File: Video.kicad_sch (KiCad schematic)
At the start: 53 parts, among them Q10 2N3904, Q6 2N3904, Q7 2N3904, Q8 2N3904, Q9 2N3904, U13 74LS04, U15 74LS86, U40 GST_SHIFTER, U41 74LS257, U42 GST_MCU, U44 74LS86, U45 74LS04

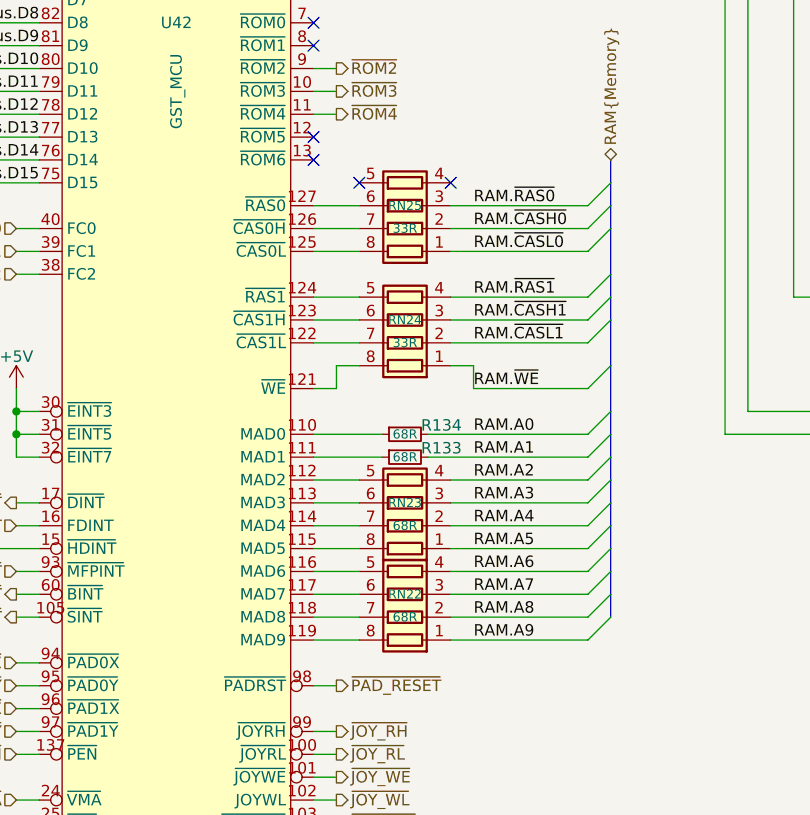
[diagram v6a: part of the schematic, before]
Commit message: motherboard: Fixed a pile of resistor network issues, and concluded initial routing of the CPU and audio amp passives
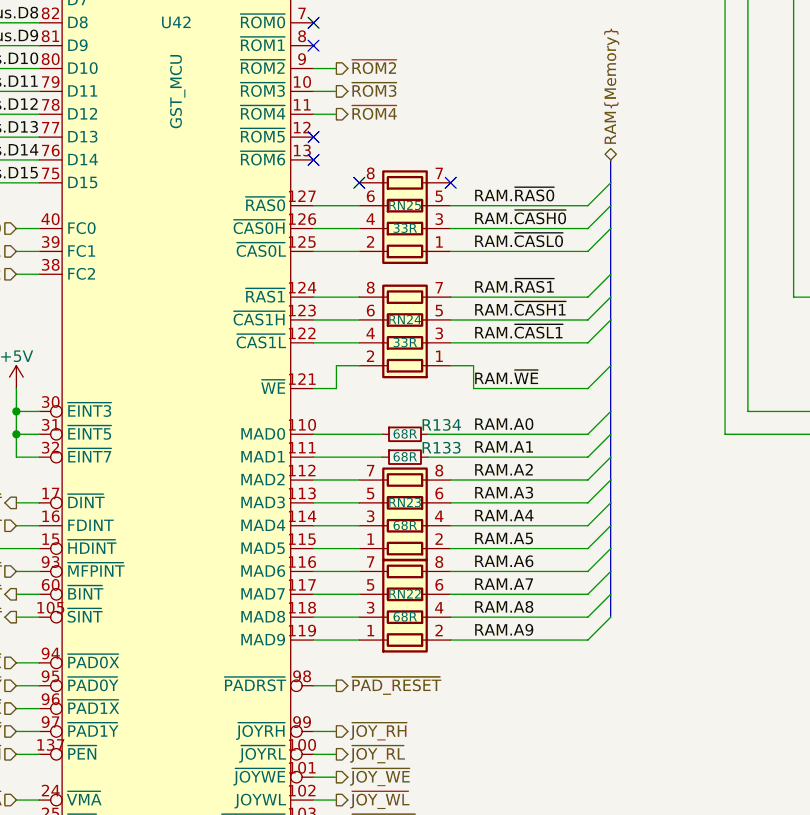
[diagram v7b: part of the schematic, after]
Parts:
- R133, R134: footprint rhais_rcl:R0603 -> rhais_rcl:R0402
- RN22, RN23, RN24, RN25: footprint rhais_rcl:R0603_Array_Concave_4 -> rhais_rcl:R0402_Array_Convex_4; symbol Device:R_Pack04 -> dragonmux:R_Pack04_OddEven
- U40: footprint Package_LCC:PLCC-84_SMD-Socket -> rhais_package-plcc:PLCC-84_SMD-Socket
- U42: footprint Package_QFP:LQFP-144_20x20mm_P0.5mm -> rhais_package-qfp:LQFP-144_20x20mm_P0.5mm
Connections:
- net RAM.A2: now also RN23.8 (R1.2); no longer RN23.4 (R4.1)
- net RAM.A3: now also RN23.6 (R3.2); no longer RN23.3 (R3.1)
- net RAM.A4: now also RN23.4 (R4.1); no longer RN23.2 (R2.1)
- net RAM.A5: now also RN23.2 (R2.1); no longer RN23.1 (R1.1)
- net RAM.A6: now also RN22.8 (R1.2); no longer RN22.4 (R4.1)
- net RAM.A7: now also RN22.6 (R3.2); no longer RN22.3 (R3.1)
- net RAM.A8: now also RN22.4 (R4.1); no longer RN22.2 (R2.1)
- net RAM.A9: now also RN22.2 (R2.1); no longer RN22.1 (R1.1)
- net RAM.~{CASH0}: now also RN25.3 (R3.1); no longer RN25.2 (R2.1)
- net RAM.~{CASH1}: now also RN24.5 (R4.2); no longer RN24.3 (R3.1)
- net RAM.~{CASL1}: now also RN24.3 (R3.1); no longer RN24.2 (R2.1)
- net RAM.~{RAS0}: now also RN25.5 (R4.2); no longer RN25.3 (R3.1)
- net RAM.~{RAS1}: now also RN24.7 (R2.2); no longer RN24.4 (R4.1)
- net at RN25.4 (R4.1): now also U42.126 (~{CAS0H})
- net at RN25.7 (R2.2): no longer U42.126 (~{CAS0H})
- net at U42.125 (~{CAS0L}): now also RN25.2 (R2.1); no longer RN25.8 (R1.2)
- net at U42.112 (MAD2): now also RN23.7 (R2.2); no longer RN23.5 (R4.2)
- net at U42.113 (MAD3): now also RN23.5 (R4.2); no longer RN23.6 (R3.2)
- net at U42.114 (MAD4): now also RN23.3 (R3.1); no longer RN23.7 (R2.2)
- net at U42.115 (MAD5): now also RN23.1 (R1.1); no longer RN23.8 (R1.2)
- net at U42.116 (MAD6): now also RN22.7 (R2.2); no longer RN22.5 (R4.2)
- net at U42.117 (MAD7): now also RN22.5 (R4.2); no longer RN22.6 (R3.2)
- net at U42.118 (MAD8): now also RN22.3 (R3.1); no longer RN22.7 (R2.2)
- net at U42.119 (MAD9): now also RN22.1 (R1.1); no longer RN22.8 (R1.2)
- net at U42.121 (~{WE}): now also RN24.2 (R2.1); no longer RN24.8 (R1.2)
- net at U42.122 (~{CAS1L}): now also RN24.4 (R4.1); no longer RN24.7 (R2.2)
- net at U42.124 (~{RAS1}): now also RN24.8 (R1.2); no longer RN24.5 (R4.2)
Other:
- moved on the sheet: RN22, RN23
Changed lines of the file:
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@@
 			)
 		)
-		(property "Footprint" "Package_LCC:PLCC-84_SMD-Socket"
+		(property "Footprint" "rhais_package-plcc:PLCC-84_SMD-Socket"
 			(at 218.44 127 90)
 			(effects
@@
 			)
 		)
+		(property "MFR" ""
+			(at 215.9 127 0)
+			(effects
+				(font
+					(size 1.27 1.27)
+				)
+				(hide yes)
+			)
+		)
+		(property "MPN" ""
+			(at 215.9 127 0)
+			(effects
+				(font
+					(size 1.27 1.27)
+				)
+				(hide yes)
+			)
+		)
+		(property "OC_FARNELL" ""
+			(at 215.9 127 0)
+			(effects
+				(font
+					(size 1.27 1.27)
+				)
+				(hide yes)
+			)
+		)
 		(pin "61"
 		)
@@
 			)
 		)
-		(property "Footprint" "rhais_rcl:R0603"
+		(property "Footprint" "rhais_rcl:R0402"
 			(at 114.3 193.04 0)
 			(effects
@@
 	)
 	(symbol
-		(lib_id "Device:R_Pack04")
+		(lib_id "dragonmux:R_Pack04_OddEven")
 		(at 114.3 165.1 90)
 		(unit 1)
@@
 			)
 		)
-		(property "Footprint" "rhais_rcl:R0603_Array_Concave_4"
+		(property "Footprint" "rhais_rcl:R0402_Array_Convex_4"
 			(at 114.3 158.115 90)
 			(effects
@@
 		)
 		(property "Description" "4 resistor network, parallel topology"
-			(at 114.3 165.1 0)
+			(at 127 166.37 0)
 			(effects
 				(font
@@
 			)
 		)
-		(property "Footprint" "Package_QFP:LQFP-144_20x20mm_P0.5mm"
+		(property "Footprint" "rhais_package-qfp:LQFP-144_20x20mm_P0.5mm"
 			(at 91.694 152.4 90)
 			(effects
@@
 			)
 		)
+		(property "MFR" ""
+			(at 88.9 152.4 0)
+			(effects
+				(font
+					(size 1.27 1.27)
+				)
+				(hide yes)
+			)
+		)
+		(property "MPN" ""
+			(at 88.9 152.4 0)
+			(effects
+				(font
+					(size 1.27 1.27)
+				)
+				(hide yes)
+			)
+		)
+		(property "OC_FARNELL" ""
+			(at 88.9 152.4 0)
+			(effects
+				(font
+					(size 1.27 1.27)
+				)
+				(hide yes)
+			)
+		)
 		(pin "55"
 		)
@@
 	)
 	(symbol
-		(lib_id "Device:R_Pack04")
+		(lib_id "dragonmux:R_Pack04_OddEven")
 		(at 114.3 177.8 90)
 		(unit 1)
@@
 			)
 		)
-		(property "Footprint" "rhais_rcl:R0603_Array_Concave_4"
+		(property "Footprint" "rhais_rcl:R0402_Array_Convex_4"
 			(at 114.3 170.815 90)
 			(effects
@@
 		)
 		(property "Description" "4 resistor network, parallel topology"
-			(at 114.3 177.8 0)
+			(at 127 179.07 0)
 			(effects
 				(font
@@
 	)
 	(symbol
-		(lib_id "Device:R_Pack04")
-		(at 114.3 198.12 90)
+		(lib_id "dragonmux:R_Pack04_OddEven")
+		(at 114.3 198.12 270)
+		(mirror x)
 		(unit 1)
 		(exclude_from_sim no)
@@
 			)
 		)
-		(property "Footprint" "rhais_rcl:R0603_Array_Concave_4"
+		(property "Footprint" "rhais_rcl:R0402_Array_Convex_4"
 			(at 114.3 191.135 90)
 			(effects
@@
 		)
 		(property "Description" "4 resistor network, parallel topology"
-			(at 114.3 198.12 0)
+			(at 101.6 199.39 0)
 			(effects
 				(font
@@
 			)
 		)
-		(property "Footprint" "rhais_rcl:R0603"
+		(property "Footprint" "rhais_rcl:R0402"
 			(at 114.3 190.5 0)
 			(effects
@@
 	)
 	(symbol
-		(lib_id "Device:R_Pack04")
-		(at 114.3 208.28 90)
+		(lib_id "dragonmux:R_Pack04_OddEven")
+		(at 114.3 208.28 270)
+		(mirror x)
 		(unit 1)
 		(exclude_from_sim no)
@@
 			)
 		)
-		(property "Footprint" "rhais_rcl:R0603_Array_Concave_4"
+		(property "Footprint" "rhais_rcl:R0402_Array_Convex_4"
 			(at 114.3 201.295 90)
 			(effects
@@
 		)
 		(property "Description" "4 resistor network, parallel topology"
-			(at 114.3 208.28 0)
+			(at 101.6 209.55 0)
 			(effects
 				(font

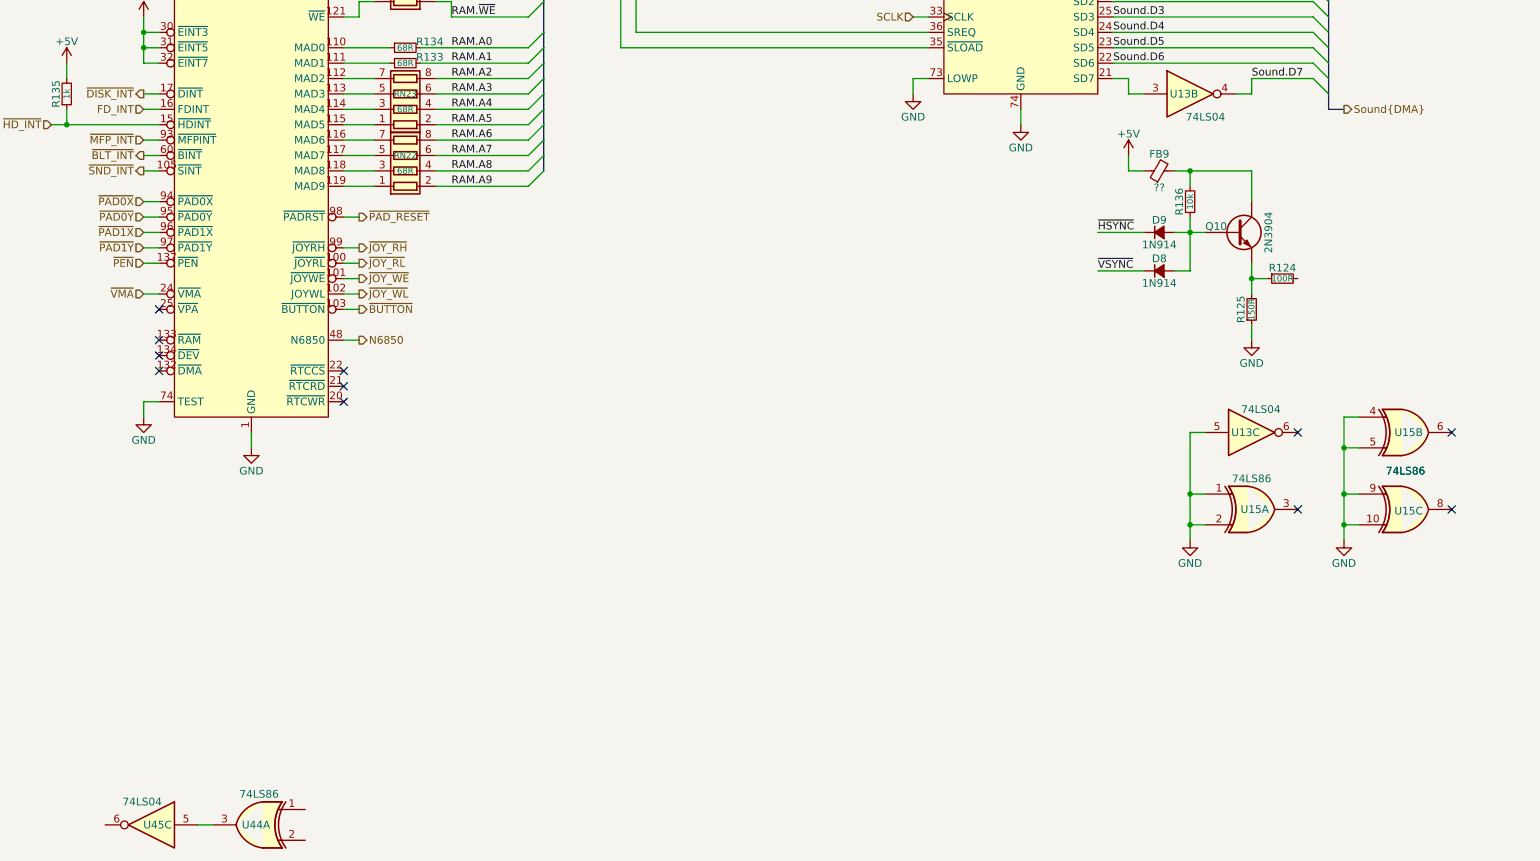
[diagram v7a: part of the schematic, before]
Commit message: motherboard: Added packaging and ordering information for many of the 7400 logic parts and the DACs
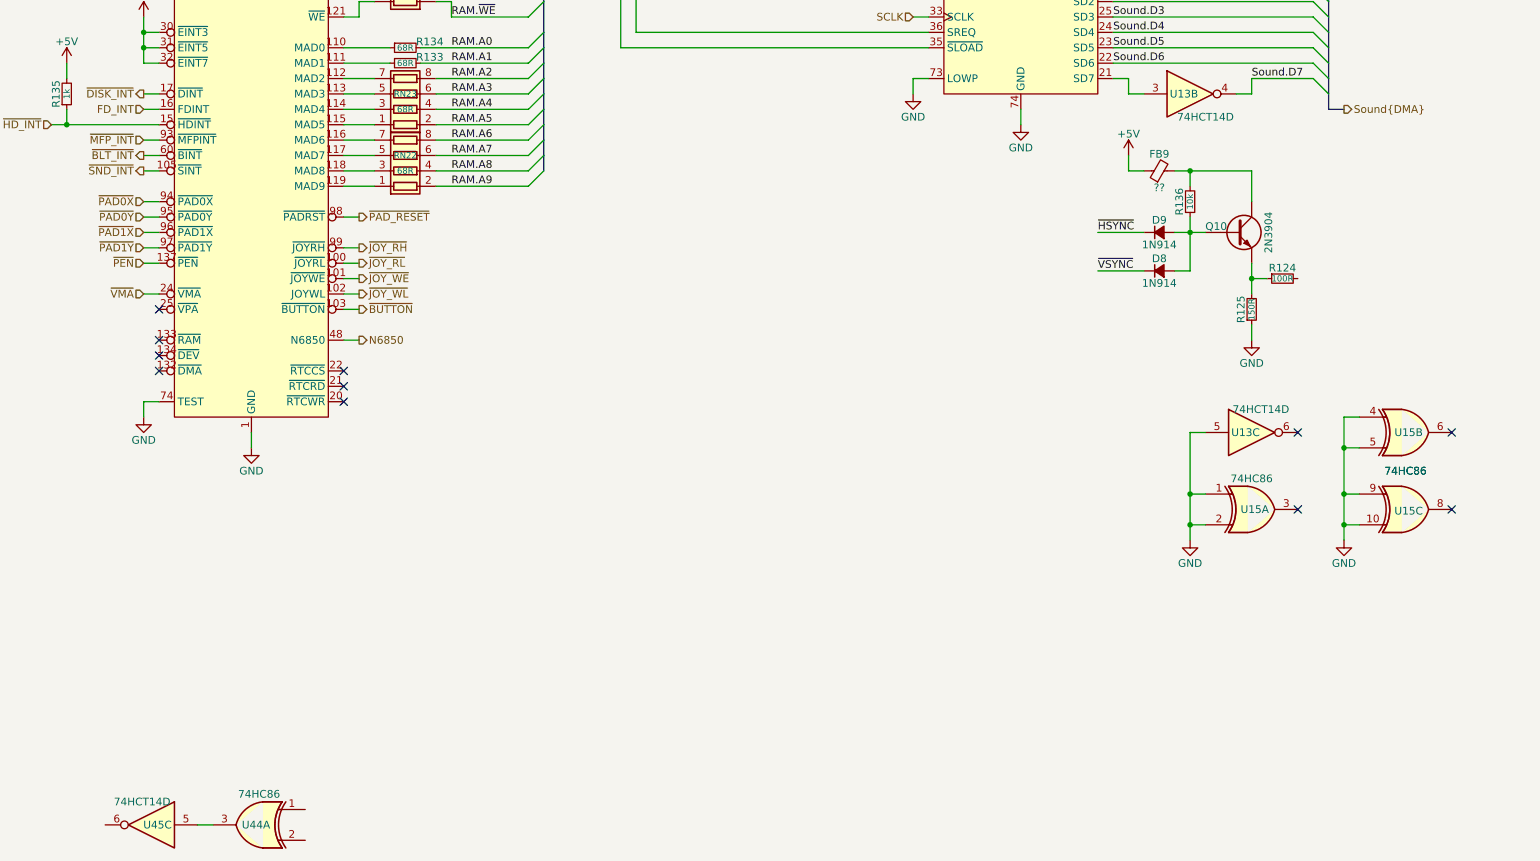
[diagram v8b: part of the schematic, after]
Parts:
- U13, U45: value 74LS04 -> 74HCT14D
- U15, U44: value 74LS86 -> 74HC86; footprint (none) -> rhais_package-smd:SO-14_3.9x8.65mm_P1.27mm; MFR (none) -> Nexperia; MPN (none) -> 74HC86D,653; OC_FARNELL (none) -> 1085331
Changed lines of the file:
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@@
 			)
 		)
-		(property "Value" "74LS04"
+		(property "Value" "74HCT14D"
 			(at 70.866 314.96 0)
 			(effects
@@
 			)
 		)
-		(property "Value" "74LS86"
+		(property "Value" "74HC86"
 			(at 254 261.62 0)
 			(effects
@@
 			)
 		)
-		(property "Footprint" ""
+		(property "Footprint" "rhais_package-smd:SO-14_3.9x8.65mm_P1.27mm"
 			(at 254 266.7 0)
 			(effects
@@
 			)
 		)
-		(property "Datasheet" "74xx/74ls86.pdf"
+		(property "Datasheet" "https://assets.nexperia.com/documents/data-sheet/74HC_HCT86.pdf"
 			(at 254 266.7 0)
 			(effects
@@
 			)
 		)
+		(property "MFR" "Nexperia"
+			(at 254 266.7 0)
+			(effects
+				(font
+					(size 1.27 1.27)
+				)
+				(hide yes)
+			)
+		)
+		(property "MPN" "74HC86D,653"
+			(at 254 266.7 0)
+			(effects
+				(font
+					(size 1.27 1.27)
+				)
+				(hide yes)
+			)
+		)
+		(property "OC_FARNELL" "1085331"
+			(at 254 266.7 0)
+			(effects
+				(font
+					(size 1.27 1.27)
+				)
+				(hide yes)
+			)
+		)
 		(pin "12"
 		)
@@
 			)
 		)
-		(property "Value" "74LS86"
+		(property "Value" "74HC86"
 			(at 279.4 260.35 0)
 			(effects
@@
 			)
 		)
-		(property "Footprint" ""
+		(property "Footprint" "rhais_package-smd:SO-14_3.9x8.65mm_P1.27mm"
 			(at 279.4 266.7 0)
 			(effects
@@
 			)
 		)
-		(property "Datasheet" "74xx/74ls86.pdf"
+		(property "Datasheet" "https://assets.nexperia.com/documents/data-sheet/74HC_HCT86.pdf"
 			(at 279.4 266.7 0)
 			(effects
@@
 			)
 		)
+		(property "MFR" "Nexperia"
+			(at 279.4 266.7 0)
+			(effects
+				(font
+					(size 1.27 1.27)
+				)
+				(hide yes)
+			)
+		)
+		(property "MPN" "74HC86D,653"
+			(at 279.4 266.7 0)
+			(effects
+				(font
+					(size 1.27 1.27)
+				)
+				(hide yes)
+			)
+		)
+		(property "OC_FARNELL" "1085331"
+			(at 279.4 266.7 0)
+			(effects
+				(font
+					(size 1.27 1.27)
+				)
+				(hide yes)
+			)
+		)
 		(pin "12"
 		)
@@
 			)
 		)
-		(property "Value" "74LS04"
+		(property "Value" "74HCT14D"
 			(at 246.38 201.93 0)
 			(effects
@@
 			)
 		)
-		(property "Value" "74LS86"
+		(property "Value" "74HC86"
 			(at 90.17 313.69 0)
 			(effects
@@
 			)
 		)
-		(property "Footprint" ""
+		(property "Footprint" "rhais_package-smd:SO-14_3.9x8.65mm_P1.27mm"
 			(at 90.17 318.77 0)
 			(effects
@@
 			)
 		)
-		(property "Datasheet" "74xx/74ls86.pdf"
+		(property "Datasheet" "https://assets.nexperia.com/documents/data-sheet/74HC_HCT86.pdf"
 			(at 90.17 318.77 0)
 			(effects
@@
 			)
 		)
+		(property "MFR" "Nexperia"
+			(at 90.17 318.77 0)
+			(effects
+				(font
+					(size 1.27 1.27)
+				)
+				(hide yes)
+			)
+		)
+		(property "MPN" "74HC86D,653"
+			(at 90.17 318.77 0)
+			(effects
+				(font
+					(size 1.27 1.27)
+				)
+				(hide yes)
+			)
+		)
+		(property "OC_FARNELL" "1085331"
+			(at 90.17 318.77 0)
+			(effects
+				(font
+					(size 1.27 1.27)
+				)
+				(hide yes)
+			)
+		)
 		(pin "12"
 		)
@@
 			)
 		)
-		(property "Value" "74LS04"
+		(property "Value" "74HCT14D"
 			(at 255.524 250.19 0)
 			(effects
@@
 			)
 		)
-		(property "Value" "74LS86"
+		(property "Value" "74HC86"
 			(at 279.4 260.35 0)
 			(effects
@@
 			)
 		)
-		(property "Footprint" ""
+		(property "Footprint" "rhais_package-smd:SO-14_3.9x8.65mm_P1.27mm"
 			(at 279.4 254 0)
 			(effects
@@
 			)
 		)
-		(property "Datasheet" "74xx/74ls86.pdf"
+		(property "Datasheet" "https://assets.nexperia.com/documents/data-sheet/74HC_HCT86.pdf"
 			(at 279.4 254 0)
 			(effects
@@
 			(at 279.4 254 0)
 			(effects
+				(font
+					(size 1.27 1.27)
+				)
+				(hide yes)
+			)
+		)
+		(property "MFR" "Nexperia"
+			(at 279.4 254 0)
+			(effects
+				(font
+					(size 1.27 1.27)
+				)
+				(hide yes)
+			)
+		)
+		(property "MPN" "74HC86D,653"
+			(at 279.4 254 0)
+			(effects
+				(font
+					(size 1.27 1.27)
+				)
+				(hide yes)
+			)
+		)
+		(property "OC_FARNELL" "1085331"
+			(at 279.4 254 0)
+			(effects
